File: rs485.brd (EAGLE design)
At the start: 49.5 x 50.8 mm, 19 parts, among them IC1 RS485SOIC, IC2 EEPROM-I2CSMD, J1 RJ11-6X, J2 RJ11-6X, Q1 BSS123, U1 ARDUINOR3-JUSTPINS

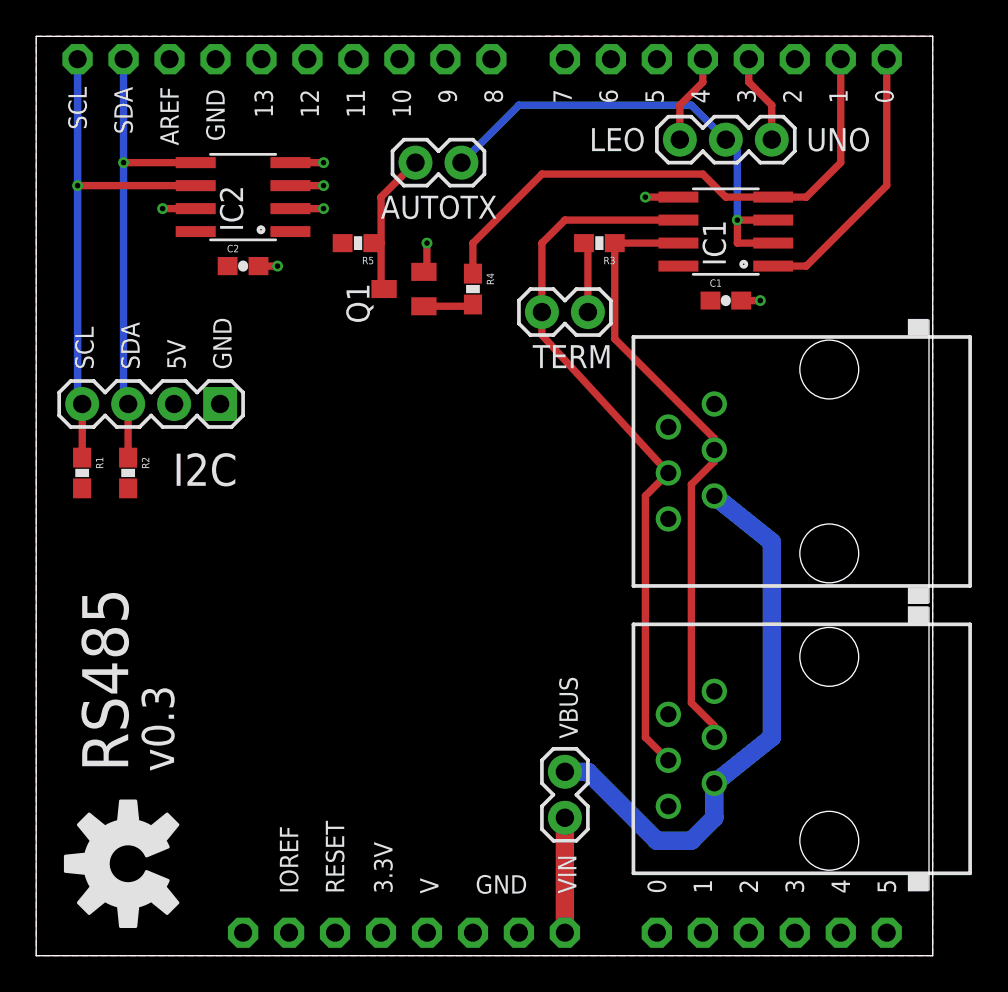
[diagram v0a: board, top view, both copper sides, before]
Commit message: corrected errant 6p6c jacks
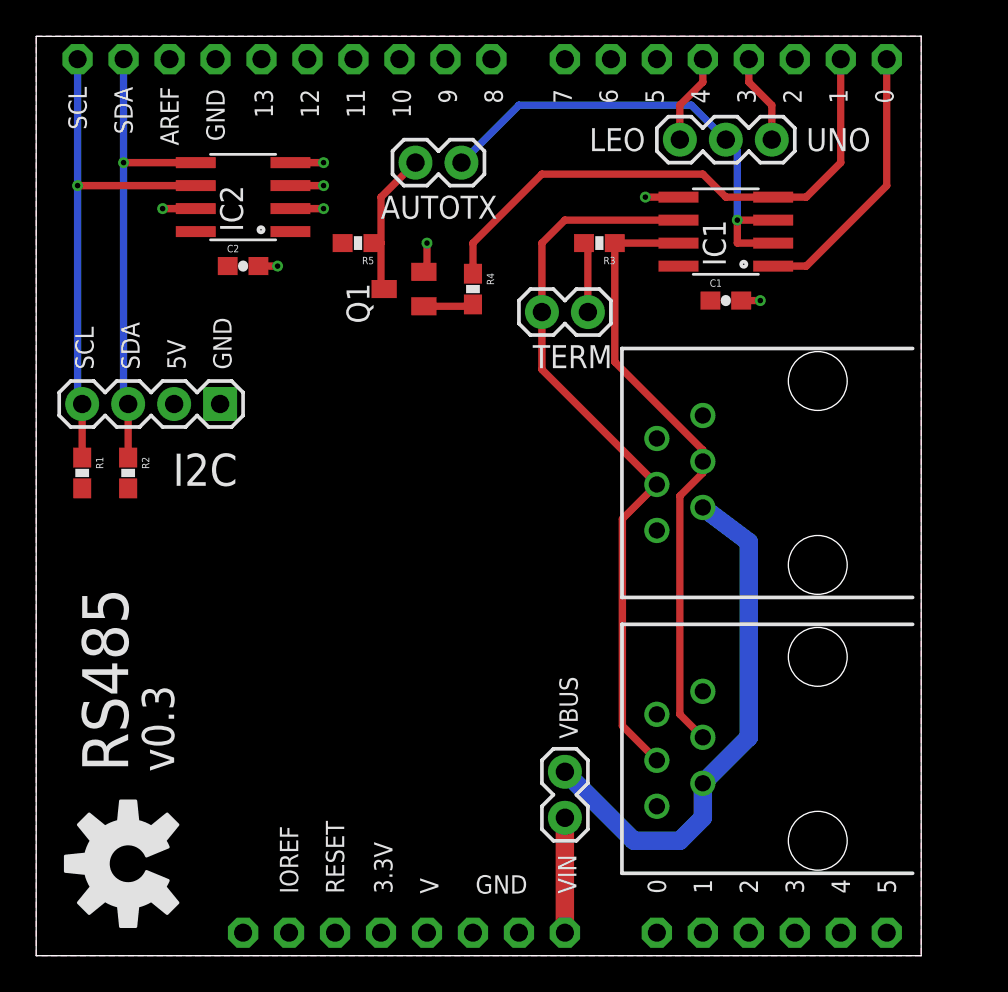
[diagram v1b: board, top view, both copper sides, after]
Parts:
- moved J1 0.90 mm to (43.2, 26.7)
- moved J2 0.63 mm to (43.2, 11.4)
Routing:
- net VBUS: track 31.2 -> 29.2 mm
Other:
- board size 49.5 x 50.8 mm -> 48.9 x 50.8 mm
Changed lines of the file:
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@@
 <board>
 <plain>
-<wire x1="0" y1="0" x2="49.53" y2="0" width="0" layer="20"/>
-<wire x1="49.53" y1="0" x2="49.53" y2="50.8" width="0" layer="20"/>
-<wire x1="49.53" y1="50.8" x2="0" y2="50.79" width="0" layer="20"/>
+<wire x1="0" y1="0" x2="48.895" y2="0" width="0" layer="20"/>
+<wire x1="48.895" y1="0" x2="48.895" y2="50.8" width="0" layer="20"/>
+<wire x1="48.895" y1="50.8" x2="0" y2="50.79" width="0" layer="20"/>
 <wire x1="0" y1="50.79" x2="0" y2="0" width="0" layer="20"/>
 <text x="5.08" y="10.16" size="2.54" layer="21" font="vector" rot="R90">RS485</text>
@@
 <element name="U1" library="arduino-pins" package="ARDUINOR3" value="ARDUINOR3-JUSTPINS" x="0" y="0"/>
 <element name="C1" library="SparkFun-Passives" package="0603-CAP" value="0.1uF" x="38.1" y="36.195"/>
-<element name="J1" library="con-tycoelectronics" package="RJ11-NO_SHIELD" value="RJ11-6X" x="43.815" y="27.305" smashed="yes" rot="R90">
-<attribute name="OC_NEWARK" value="16R6089" x="43.815" y="27.305" size="1.778" layer="27" rot="R90" display="off"/>
-<attribute name="MPN" value="RJ11-6X" x="43.815" y="27.305" size="1.778" layer="27" rot="R90" display="off"/>
-<attribute name="MF" value="" x="43.815" y="27.305" size="1.778" layer="27" rot="R90" display="off"/>
-<attribute name="OC_FARNELL" value="unknown" x="43.815" y="27.305" size="1.778" layer="27" rot="R90" display="off"/>
-</element>
-<element name="J2" library="con-tycoelectronics" package="RJ11-NO_SHIELD" value="RJ11-6X" x="43.815" y="11.43" smashed="yes" rot="R90">
-<attribute name="OC_NEWARK" value="16R6089" x="43.815" y="11.43" size="1.778" layer="27" rot="R90" display="off"/>
-<attribute name="MPN" value="RJ11-6X" x="43.815" y="11.43" size="1.778" layer="27" rot="R90" display="off"/>
-<attribute name="MF" value="" x="43.815" y="11.43" size="1.778" layer="27" rot="R90" display="off"/>
-<attribute name="OC_FARNELL" value="unknown" x="43.815" y="11.43" size="1.778" layer="27" rot="R90" display="off"/>
+<element name="J1" library="con-tycoelectronics" package="RJ11-NO_SHIELD" value="RJ11-6X" x="43.18" y="26.67" smashed="yes" rot="R90">
+<attribute name="OC_NEWARK" value="16R6089" x="43.18" y="26.67" size="1.778" layer="27" rot="R90" display="off"/>
+<attribute name="MPN" value="RJ11-6X" x="43.18" y="26.67" size="1.778" layer="27" rot="R90" display="off"/>
+<attribute name="MF" value="" x="43.18" y="26.67" size="1.778" layer="27" rot="R90" display="off"/>
+<attribute name="OC_FARNELL" value="unknown" x="43.18" y="26.67" size="1.778" layer="27" rot="R90" display="off"/>
+</element>
+<element name="J2" library="con-tycoelectronics" package="RJ11-NO_SHIELD" value="RJ11-6X" x="43.18" y="11.43" smashed="yes" rot="R90">
+<attribute name="OC_NEWARK" value="16R6089" x="43.18" y="11.43" size="1.778" layer="27" rot="R90" display="off"/>
+<attribute name="MPN" value="RJ11-6X" x="43.18" y="11.43" size="1.778" layer="27" rot="R90" display="off"/>
+<attribute name="MF" value="" x="43.18" y="11.43" size="1.778" layer="27" rot="R90" display="off"/>
+<attribute name="OC_FARNELL" value="unknown" x="43.18" y="11.43" size="1.778" layer="27" rot="R90" display="off"/>
 </element>
 <element name="JP1" library="SparkFun-Connectors" package="1X03" value="" x="35.56" y="45.085" smashed="yes">
@@
 <vertex x="0" y="0"/>
 <vertex x="0" y="50.8"/>
-<vertex x="49.53" y="50.8"/>
-<vertex x="49.53" y="0"/>
+<vertex x="48.895" y="50.8"/>
+<vertex x="48.895" y="0"/>
 </polygon>
 <contactref element="U1" pad="GND"/>
@@
 <vertex x="0" y="0"/>
 <vertex x="0" y="50.8"/>
-<vertex x="49.53" y="50.8"/>
-<vertex x="49.53" y="0"/>
+<vertex x="48.895" y="50.8"/>
+<vertex x="48.895" y="0"/>
 </polygon>
 <contactref element="R5" pad="2"/>
@@
 <contactref element="J2" pad="4"/>
 <contactref element="R3" pad="1"/>
-<wire x1="37.465" y1="27.94" x2="37.465" y2="28.575" width="0.4064" layer="1"/>
-<wire x1="37.465" y1="28.575" x2="31.965" y2="34.075" width="0.4064" layer="1"/>
-<wire x1="37.465" y1="12.065" x2="37.465" y2="12.7" width="0.4064" layer="1"/>
-<wire x1="37.465" y1="12.7" x2="36.195" y2="13.97" width="0.4064" layer="1"/>
-<wire x1="37.465" y1="27.94" x2="37.465" y2="27.305" width="0.4064" layer="1"/>
-<wire x1="37.465" y1="27.305" x2="36.195" y2="26.035" width="0.4064" layer="1"/>
-<wire x1="36.195" y1="26.035" x2="36.195" y2="13.97" width="0.4064" layer="1"/>
 <wire x1="35.4838" y1="39.37" x2="31.965" y2="39.37" width="0.4064" layer="1"/>
-<wire x1="31.965" y1="34.075" x2="31.965" y2="39.37" width="0.4064" layer="1"/>
+<wire x1="31.965" y1="32.805" x2="31.965" y2="39.37" width="0.4064" layer="1"/>
+<wire x1="31.965" y1="32.805" x2="36.83" y2="27.94" width="0.4064" layer="1"/>
+<wire x1="36.83" y1="27.94" x2="36.83" y2="27.305" width="0.4064" layer="1"/>
+<wire x1="36.83" y1="27.305" x2="36.83" y2="26.67" width="0.4064" layer="1"/>
+<wire x1="36.83" y1="26.67" x2="35.56" y2="25.4" width="0.4064" layer="1"/>
+<wire x1="35.56" y1="25.4" x2="35.56" y2="13.335" width="0.4064" layer="1"/>
+<wire x1="35.56" y1="13.335" x2="36.83" y2="12.065" width="0.4064" layer="1"/>
 </signal>
 <signal name="A">
@@
 <contactref element="J2" pad="3"/>
 <contactref element="TERM" pad="2"/>
-<wire x1="34.925" y1="10.795" x2="33.655" y2="12.065" width="0.4064" layer="1"/>
-<wire x1="33.655" y1="12.065" x2="33.655" y2="25.4" width="0.4064" layer="1"/>
-<wire x1="33.655" y1="25.4" x2="34.925" y2="26.67" width="0.4064" layer="1"/>
 <wire x1="27.94" y1="35.56" x2="27.94" y2="39.37" width="0.4064" layer="1"/>
 <wire x1="27.94" y1="39.37" x2="29.21" y2="40.64" width="0.4064" layer="1"/>
 <wire x1="29.21" y1="40.64" x2="35.4838" y2="40.64" width="0.4064" layer="1"/>
-<wire x1="27.94" y1="35.56" x2="27.94" y2="34.29" width="0.4064" layer="1"/>
-<wire x1="27.94" y1="34.29" x2="34.925" y2="26.67" width="0.4064" layer="1"/>
+<wire x1="27.94" y1="35.56" x2="27.94" y2="32.385" width="0.4064" layer="1"/>
+<wire x1="27.94" y1="32.385" x2="34.29" y2="26.035" width="0.4064" layer="1"/>
+<wire x1="34.29" y1="26.035" x2="32.385" y2="24.13" width="0.4064" layer="1"/>
+<wire x1="32.385" y1="24.13" x2="32.385" y2="12.7" width="0.4064" layer="1"/>
+<wire x1="32.385" y1="12.7" x2="34.29" y2="10.795" width="0.4064" layer="1"/>
 </signal>
 <signal name="SCL">
@@
 <contactref element="J1" pad="2"/>
 <contactref element="VBUS" pad="1"/>
-<wire x1="37.465" y1="25.4" x2="40.64" y2="22.86" width="1.016" layer="16"/>
-<wire x1="40.64" y1="22.86" x2="40.64" y2="12.065" width="1.016" layer="16"/>
-<wire x1="40.64" y1="12.065" x2="37.465" y2="9.525" width="1.016" layer="16"/>
-<wire x1="34.29" y1="6.35" x2="36.195" y2="6.35" width="1.016" layer="16"/>
-<wire x1="36.195" y1="6.35" x2="37.465" y2="7.62" width="1.016" layer="16"/>
-<wire x1="37.465" y1="7.62" x2="37.465" y2="9.525" width="1.016" layer="16"/>
-<wire x1="29.21" y1="10.16" x2="30.48" y2="10.16" width="1.016" layer="16"/>
-<wire x1="30.48" y1="10.16" x2="34.29" y2="6.35" width="1.016" layer="16"/>
+<wire x1="36.83" y1="24.765" x2="39.37" y2="22.86" width="1.016" layer="16"/>
+<wire x1="39.37" y1="22.86" x2="39.37" y2="12.065" width="1.016" layer="16"/>
+<wire x1="39.37" y1="12.065" x2="36.83" y2="9.525" width="1.016" layer="16"/>
+<wire x1="33.02" y1="6.35" x2="35.56" y2="6.35" width="1.016" layer="16"/>
+<wire x1="35.56" y1="6.35" x2="36.83" y2="7.62" width="1.016" layer="16"/>
+<wire x1="36.83" y1="7.62" x2="36.83" y2="9.525" width="1.016" layer="16"/>
+<wire x1="29.21" y1="10.16" x2="33.02" y2="6.35" width="1.016" layer="16"/>
 </signal>
 <signal name="VIN">
